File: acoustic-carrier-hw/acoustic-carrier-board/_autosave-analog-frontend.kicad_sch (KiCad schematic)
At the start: 96 parts, among them J1001 BWU.FL-IPEX1, J1002 BWU.FL-IPEX1, J1003 BWU.FL-IPEX1, J1004 BWU.FL-IPEX1, J1005 BWU.FL-IPEX1, J1006 BWU.FL-IPEX1, J1007 8P8C_Shielded, J1008 BWU.FL-IPEX1, U1001 MS9280, U1002 THS4521IDGK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

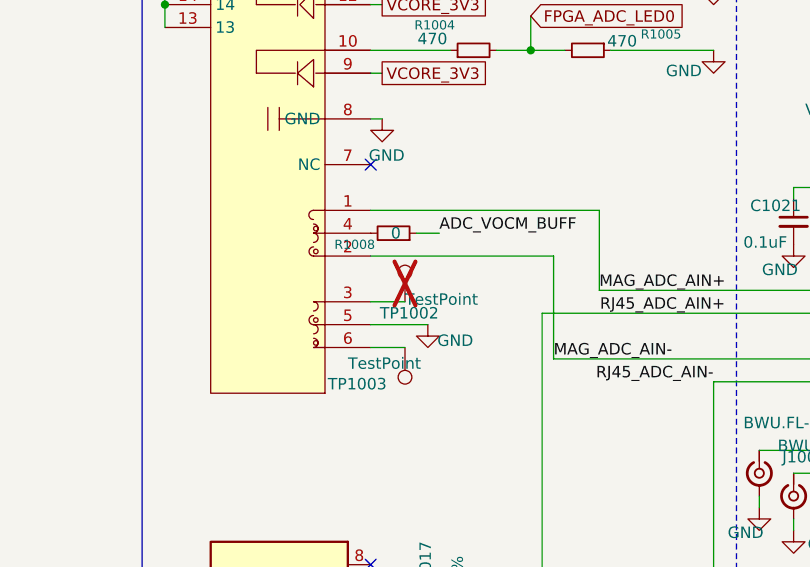
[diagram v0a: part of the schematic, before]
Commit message: [carrier] Finished rough layout, p (put together according to component category
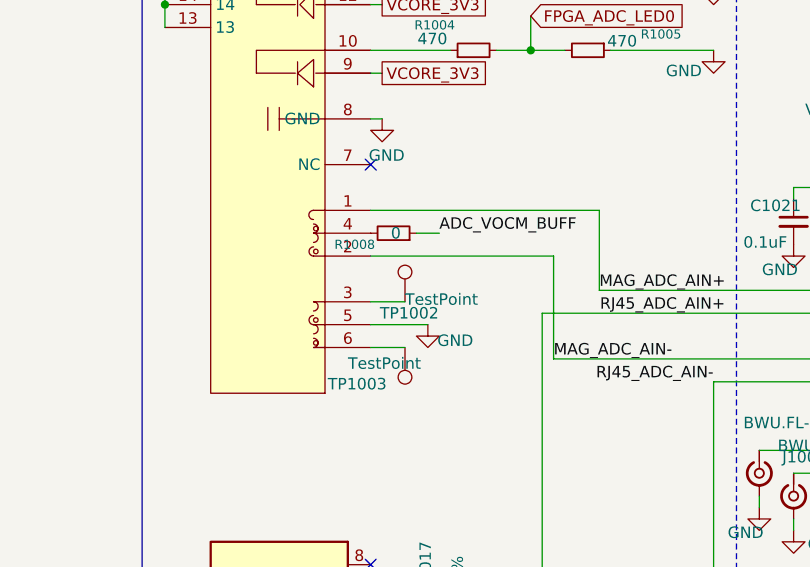
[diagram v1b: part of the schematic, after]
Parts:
- TP1002: now fitted
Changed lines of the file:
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@@
 		(in_bom yes)
 		(on_board yes)
-		(dnp yes)
+		(dnp no)
 		(property "Reference" "TP1002"
 			(at 40.386 83.82 0)
